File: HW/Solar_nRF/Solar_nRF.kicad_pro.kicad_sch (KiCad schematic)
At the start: 42 parts, among them J10 Conn_01x02, J11 Conn_01x02, J2 Conn_01x04, J4 Conn_01x02, J5 Conn_01x02, J6 Conn_01x04, J7 Conn_01x04, Q1 IRLML6402, Q2 IRLML6402, Q3 IRLML6244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

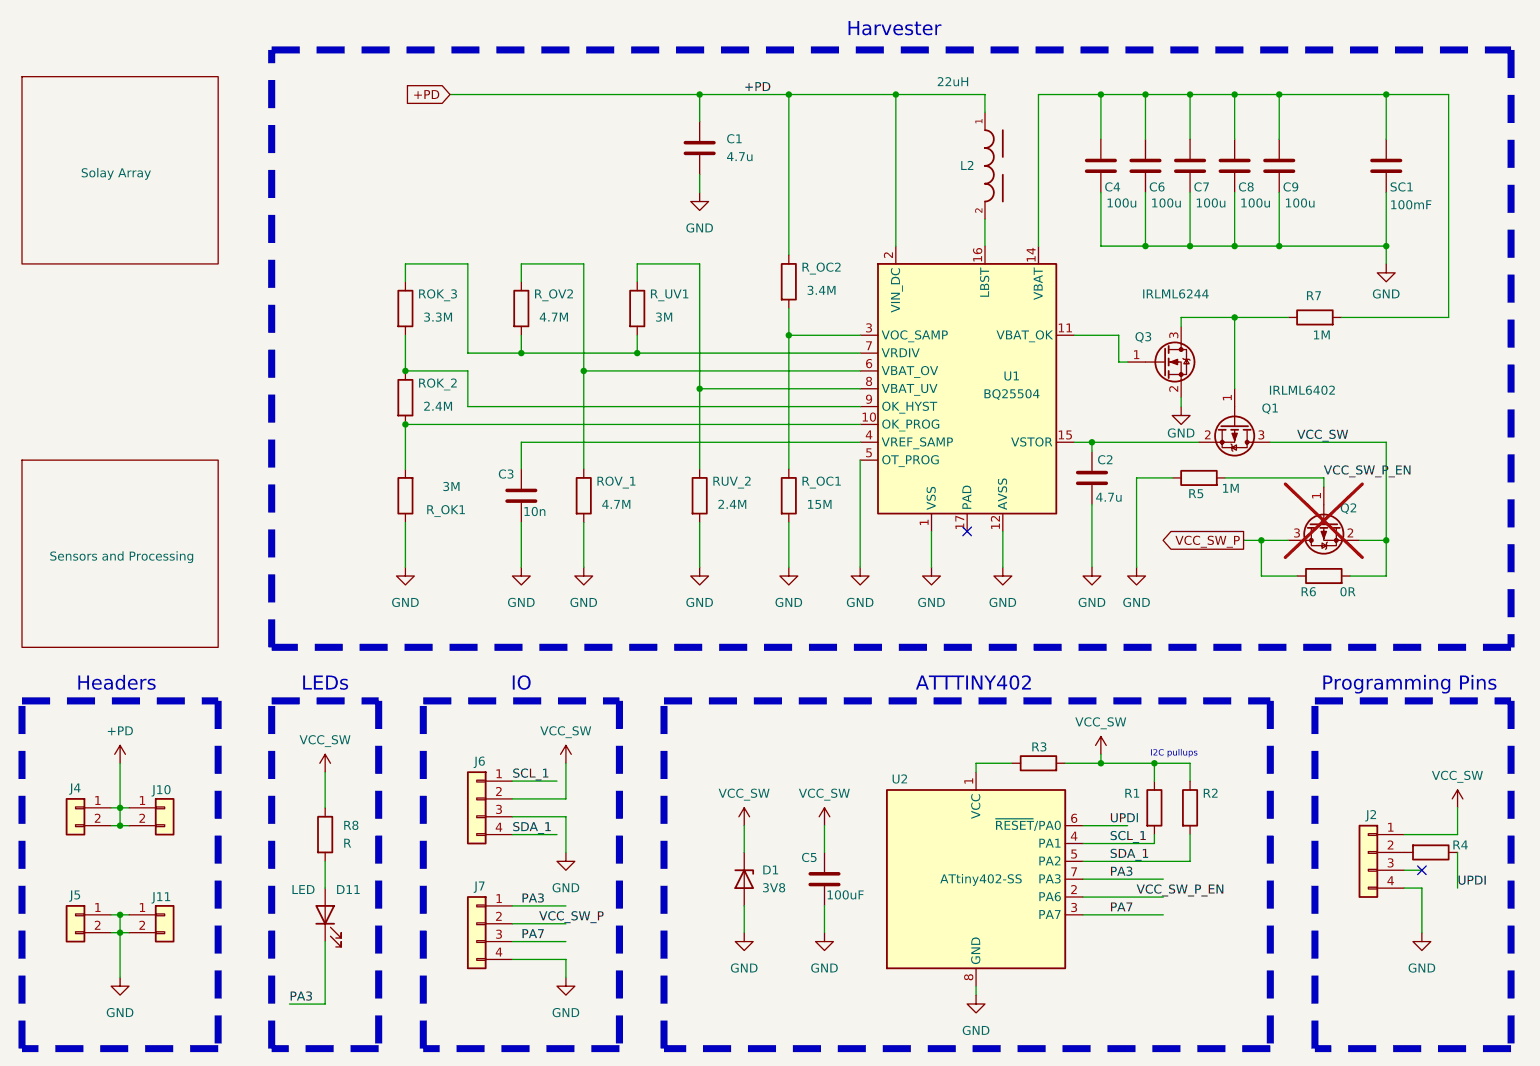
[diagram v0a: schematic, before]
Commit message: Updated SCH & PCB based with fixes found during development
Inverted bat_ok signal
Cleaned up layout, removing solar array and replacing with a single photodiode
Connected nRF to +V programming pad
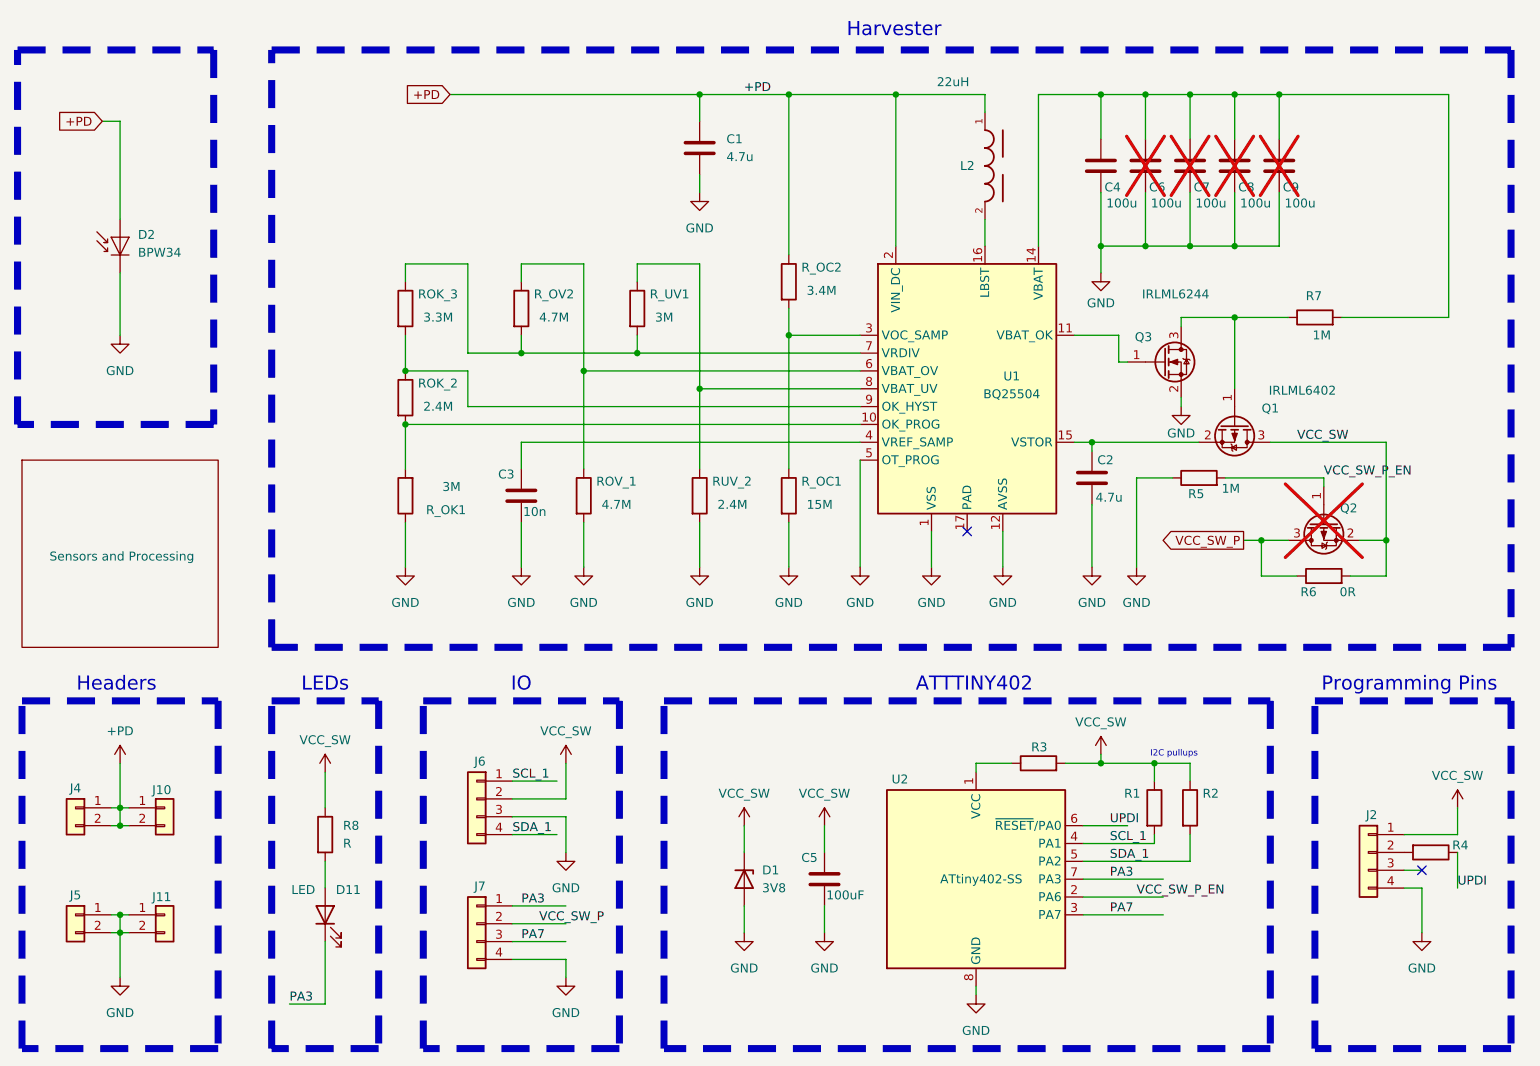
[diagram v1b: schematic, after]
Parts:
- removed SC1: 100mF, FT0H104ZF:CAPPRD508W154D1200H850, symbol Device:C
- added D2: BPW34, OptoDevice:Osram_DIL2_4.3x4.65mm_P5.08mm, symbol Sensor_Optical:BPW34
- C6, C7, C8, C9: now not fitted
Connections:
- net +PD: now also D2.2 (A)
- net GND: now also D2.1 (K)
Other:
- removed sheet Solay Array

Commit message: start
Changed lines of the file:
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@@
 (kicad_sch
-	(version 20231120)
+	(version 20250114)
 	(generator "eeschema")
-	(generator_version "8.0")
+	(generator_version "9.0")
 	(paper "A4")
 	(title_block
@@
 		(rev "1")
 	)
+	(rectangle
+		(start 77.47 113.03)
+		(end 92.71 162.56)
+		(stroke
+			(width 1)
+			(type dash)
+			(color 255 0 255 0.6)
+		)
+		(fill
+			(type none)
+		)
+	)
+	(rectangle
+		(start 77.47 20.32)
+		(end 254 105.41)
+		(stroke
+			(width 1)
+			(type dash)
+			(color 0 255 255 0.5)
+		)
+		(fill
+			(type none)
+		)
+	)
+	(rectangle
+		(start 226.06 113.03)
+		(end 254 162.56)
+		(stroke
+			(width 1)
+			(type dash)
+			(color 255 0 255 0.6)
+		)
+		(fill
+			(type none)
+		)
+	)
+	(rectangle
+		(start 41.275 20.32)
+		(end 69.215 73.66)
+		(stroke
+			(width 1)
+			(type dash)
+			(color 255 0 255 0.6)
+		)
+		(fill
+			(type none)
+		)
+	)
+	(rectangle
+		(start 99.06 113.03)
+		(end 127 162.56)
+		(stroke
+			(width 1)
+			(type dash)
+			(color 255 0 255 0.6)
+		)
+		(fill
+			(type none)
+		)
+	)
+	(rectangle
+		(start 41.91 113.03)
+		(end 69.85 162.56)
+		(stroke
+			(width 1)
+			(type dash)
+			(color 255 0 255 0.6)
+		)
+		(fill
+			(type none)
+		)
+	)
+	(rectangle
+		(start 133.35 113.03)
+		(end 219.71 162.56)
+		(stroke
+			(width 1)
+			(type dash)
+			(color 255 0 255 0.6)
+		)
+		(fill
+			(type none)
+		)
+	)
+	(text "Programming Pins"
+		(exclude_from_sim no)
+		(at 239.522 110.744 0)
+		(effects
+			(font
+				(size 2 2)
+			)
+		)
+	)
+	(text "I2C pullups"
+		(exclude_from_sim no)
+		(at 205.994 120.65 0)
+		(effects
+			(font
+				(size 0.889 0.889)
+			)
+		)
+	)
+	(text "IO"
+		(exclude_from_sim no)
+		(at 113.03 110.744 0)
+		(effects
+			(font
+				(size 2 2)
+			)
+		)
+	)
+	(text "ATTTINY402"
+		(exclude_from_sim no)
+		(at 177.546 110.744 0)
+		(effects
+			(font
+				(size 2 2)
+			)
+		)
+	)
+	(text "Harvester"
+		(exclude_from_sim no)
+		(at 166.116 17.526 0)
+		(effects
+			(font
+				(size 2 2)
+			)
+		)
+	)
+	(text "Headers"
+		(exclude_from_sim no)
+		(at 55.372 110.744 0)
+		(effects
+			(font
+				(size 2 2)
+			)
+		)
+	)
+	(text "LEDs\n"
+		(exclude_from_sim no)
+		(at 85.09 110.744 0)
+		(effects
+			(font
+				(size 2 2)
+			)
+		)
+	)
 	(junction
 		(at 214.63 26.67)
@@
 		)
 	)
-	(rectangle
-		(start 77.47 113.03)
-		(end 92.71 162.56)
-		(stroke
-			(width 1)
-			(type dash)
-			(color 255 0 255 0.6)
-		)
-		(fill
-			(type none)
-		)
-	)
-	(rectangle
-		(start 77.47 20.32)
-		(end 254 105.41)
-		(stroke
-			(width 1)
-			(type dash)
-			(color 0 255 255 0.5)
-		)
-		(fill
-			(type none)
-		)
-	)
-	(rectangle
-		(start 226.06 113.03)
-		(end 254 162.56)
-		(stroke
-			(width 1)
-			(type dash)
-			(color 255 0 255 0.6)
-		)
-		(fill
-			(type none)
-		)
-	)
-	(rectangle
-		(start 41.275 20.32)
-		(end 69.215 73.66)
-		(stroke
-			(width 1)
-			(type dash)
-			(color 255 0 255 0.6)
-		)
-		(fill
-			(type none)
-		)
-	)
-	(rectangle
-		(start 99.06 113.03)
-		(end 127 162.56)
-		(stroke
-			(width 1)
-			(type dash)
-			(color 255 0 255 0.6)
-		)
-		(fill
-			(type none)
-		)
-	)
-	(rectangle
-		(start 41.91 113.03)
-		(end 69.85 162.56)
-		(stroke
-			(width 1)
-			(type dash)
-			(color 255 0 255 0.6)
-		)
-		(fill
-			(type none)
-		)
-	)
-	(rectangle
-		(start 133.35 113.03)
-		(end 219.71 162.56)
-		(stroke
-			(width 1)
-			(type dash)
-			(color 255 0 255 0.6)
-		)
-		(fill
-			(type none)
-		)
-	)
-	(text "Programming Pins"
-		(exclude_from_sim no)
-		(at 239.522 110.744 0)
-		(effects
-			(font
-				(size 2 2)
-			)
-		)
-	)
-	(text "I2C pullups"
-		(exclude_from_sim no)
-		(at 205.994 120.65 0)
-		(effects
-			(font
-				(size 0.889 0.889)
-			)
-		)
-	)
-	(text "IO"
-		(exclude_from_sim no)
-		(at 113.03 110.744 0)
-		(effects
-			(font
-				(size 2 2)
-			)
-		)
-	)
-	(text "ATTTINY402"
-		(exclude_from_sim no)
-		(at 177.546 110.744 0)
-		(effects
-			(font
-				(size 2 2)
-			)
-		)
-	)
-	(text "Harvester"
-		(exclude_from_sim no)
-		(at 166.116 17.526 0)
-		(effects
-			(font
-				(size 2 2)
-			)
-		)
-	)
-	(text "Headers"
-		(exclude_from_sim no)
-		(at 55.372 110.744 0)
-		(effects
-			(font
-				(size 2 2)
-			)
-		)
-	)
-	(text "LEDs\n"
-		(exclude_from_sim no)
-		(at 85.09 110.744 0)
-		(effects
-			(font
-				(size 2 2)
-			)
-		)
-	)
 	(label "PA3"
 		(at 196.85 138.43 0)
@@
 		(at 41.91 78.74)
 		(size 27.94 26.67)
+		(exclude_from_sim no)
+		(in_bom yes)
+		(on_board yes)
+		(dnp no)
 		(stroke
 			(width 0.1524)
@@
 		)
 	)
+	(embedded_fonts no)
 )
